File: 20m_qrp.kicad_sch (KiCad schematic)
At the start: 55 parts, among them U1 K7812-500R3-LB, U2 K7805-500R3-LB, U3 SA612A, U4 BGA2818, U5 LTC455GW, U6 BGA2818, U7 SA612A

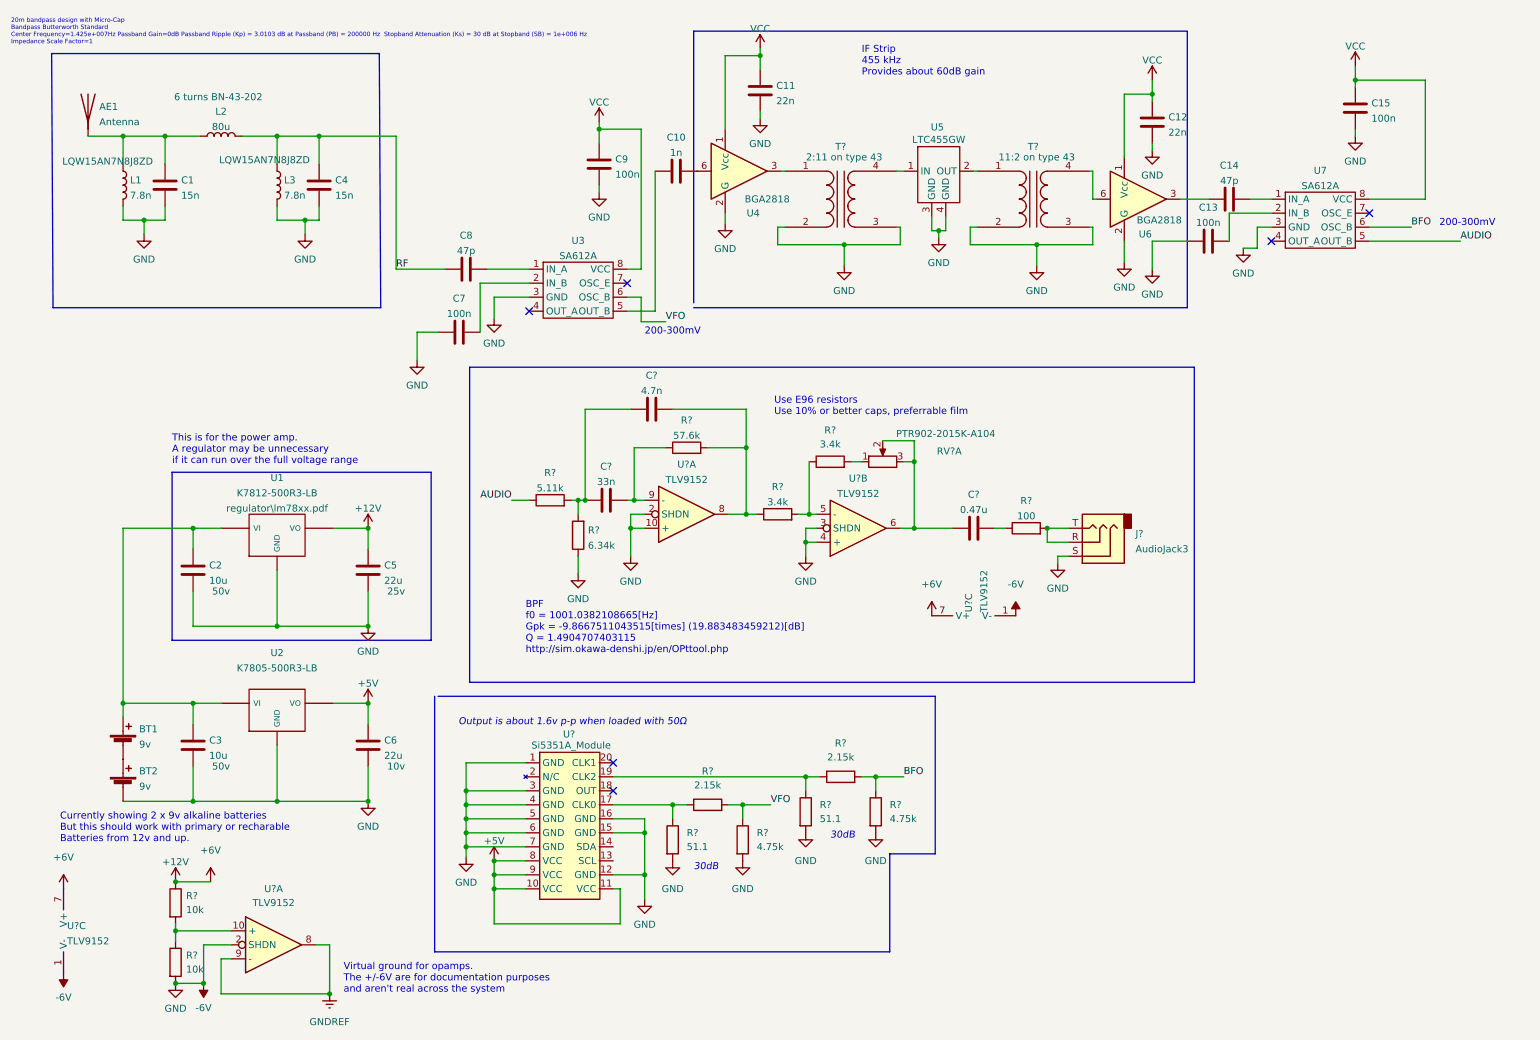
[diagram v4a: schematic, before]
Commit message: Add mic preamp and refactor schematic into hierarchical sheets
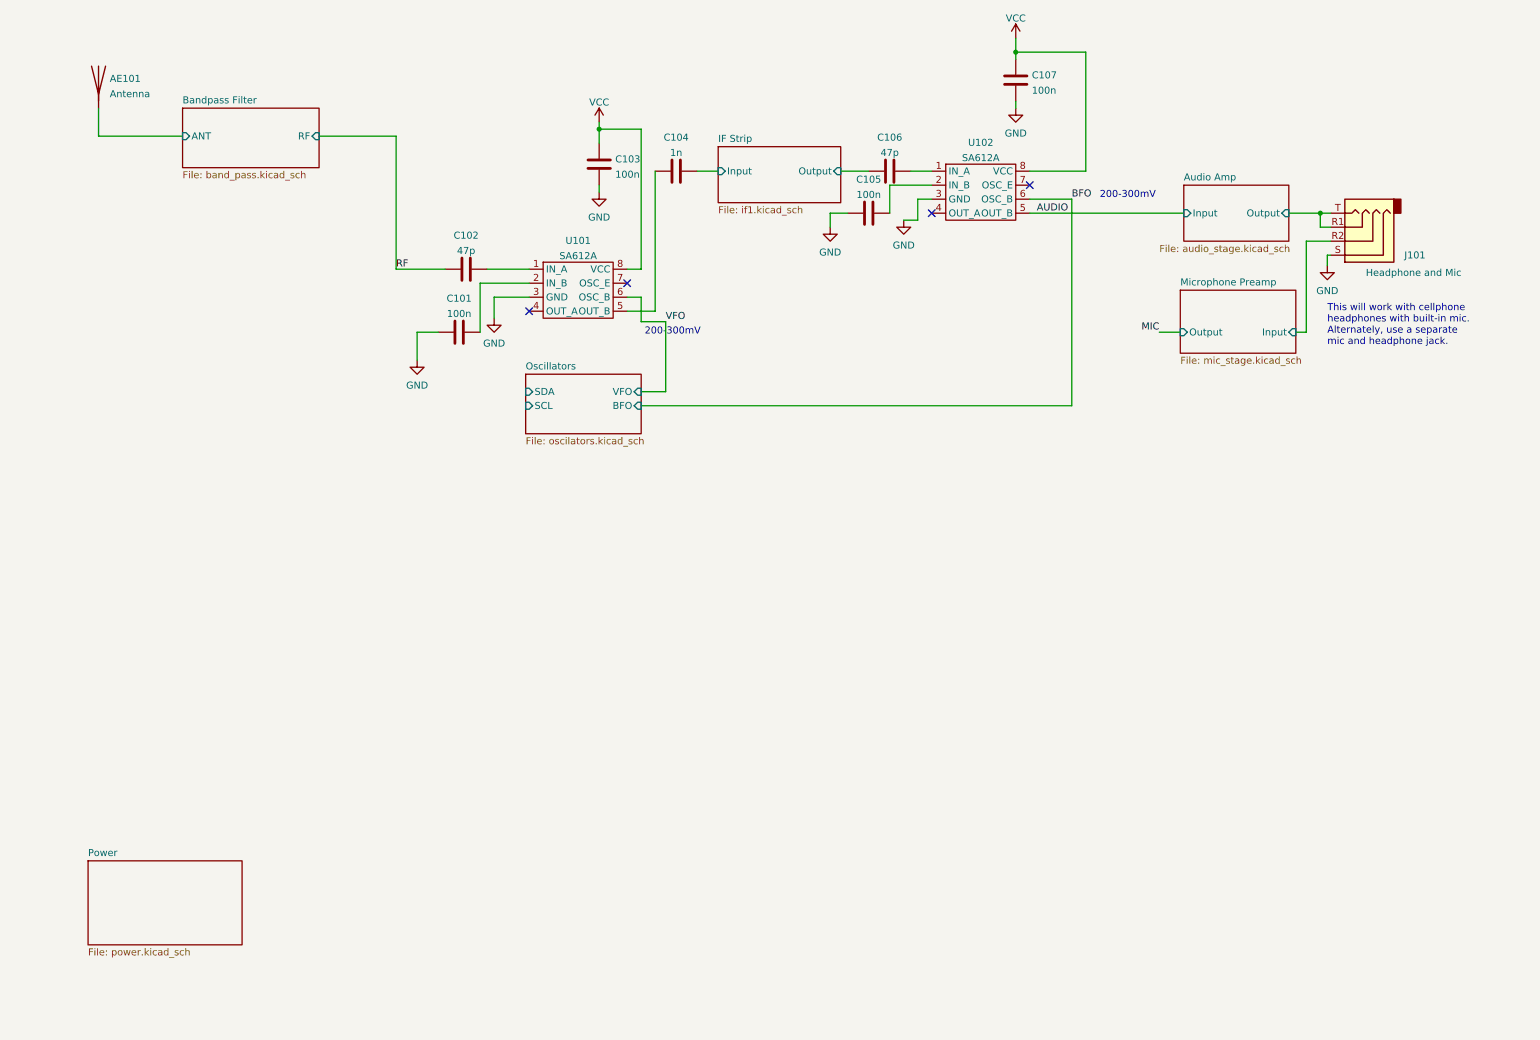
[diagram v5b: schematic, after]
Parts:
- removed AE1: Antenna, symbol Device:Antenna
- removed BT1, BT2: 9v, symbol Device:Battery_Cell
- removed C1, C4: 15n, symbol Device:C
- removed C11, C12: 22n, symbol Device:C
- removed C2, C3: 10u, symbol Device:C
- removed C5, C6: 22u, symbol Device:C
- removed C?: 33n, symbol Device:C
- removed C?: 4.7n, symbol Device:C
- removed C?: 0.47u, symbol Device:C
- removed J?: AudioJack3, symbol Connector:AudioJack3
- removed L1, L3: 7.8n, symbol Device:L
- removed L2: 80u, symbol Device:L
- removed R? (x2): 51.1, symbol Device:R
- removed R? (x2): 2.15k, symbol Device:R
- removed R? (x2): 4.75k, symbol Device:R
- removed R? (x2): 3.4k, symbol Device:R
- removed R? (x2): 10k, symbol Device:R
- removed R?: 6.34k, symbol Device:R
- removed R?: 100, symbol Device:R
- removed R?: 5.11k, symbol Device:R
- removed R?: 57.6k, symbol Device:R
- removed RV?: PTR902-2015K-A104, symbol Device:R_Potentiometer_Dual_Separate
- removed T?: 2:11 on type 43, symbol Device:Transformer_1P_1S
- removed T?: 11:2 on type 43, symbol Device:Transformer_1P_1S
- removed U1: K7812-500R3-LB, symbol regul_fixed:7805
- removed U2: K7805-500R3-LB, symbol regul_fixed:7805
- removed U4, U6: BGA2818, Package_TO_SOT_SMD:SOT-363_SC-70-6, symbol RF_Amplifier:BGA2818
- removed U5: LTC455GW, symbol components:WTL6R60427VH
- removed U? (x5): TLV9152, symbol components:TLV9152
- removed U?: Si5351A_Module, symbol components:Si5351A_Module
- added AE101: Antenna, symbol Device:Antenna
- added J101: Headphone and Mic, symbol Connector:AudioJack4
- renumbered C7 to C101, C8 to C102, C9 to C103, C10 to C104, C13 to C105, C14 to C106, C15 to C107, U3 to U101, U7 to U102
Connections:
- net IF Strip/Input: now reaches C104.2
- net IF Strip/Output: now reaches C106.1
- net -6V renamed GND
- net GND: now also J101.S
- new net Audio Amp/Output: J101.R1, J101.T
- new net Bandpass Filter/ANT: AE101.1 (A)
- new net Microphone Preamp/Input: J101.R2
- no-connect marks 6 -> 4
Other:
- added sheet Audio Amp (audio_stage.kicad_sch)
- added sheet Bandpass Filter (band_pass.kicad_sch)
- added sheet IF Strip (if1.kicad_sch)
- added sheet Microphone Preamp (mic_stage.kicad_sch)
- added sheet Oscillators (oscilators.kicad_sch)
- added sheet Power (power.kicad_sch)
- note added: "This will work with cellphone headphones with built-in mic. Alternately, use a separate mic and headphone jack."
- note removed: "20m bandpass design with Micro-Cap Bandpass Butterworth Standard Center Frequency=1.425e+007Hz Passband Gain=0dB Passband Ripple (Kp) = 3.0103 dB at Passband (PB) = 200000 Hz Stopband Attenuation (Ks) = 30 dB at Stopband (SB) = 1e+006 Hz Impedance Scale Factor=1"
- note removed: "30dB"
- note removed: "BPF f0 = 1001.0382108665[Hz] Gpk = -9.8667511043515[times] (19.883483459212)[dB] Q = 1.4904707403115 http://sim.okawa-denshi.jp/en/OPttool.php"
- note removed: "Currently showing 2 x 9v alkaline batteries But this should work with primary or recharable Batteries from 12v and up."
- note removed: "IF Strip 455 kHz Provides about 60dB gain"
- note removed: "Output is about 1.6v p-p when loaded with 50Ω"
- note removed: "This is for the power amp. A regulator may be unnecessary if it can run over the full voltage range"
- note removed: "Use E96 resistors Use 10% or better caps, preferrable film"
- note removed: "Virtual ground for opamps. The +/-6V are for documentation purposes and aren't real across the system"
- moved on the sheet: C105, C106, C107, U102
